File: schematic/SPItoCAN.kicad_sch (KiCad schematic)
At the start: 13 parts, among them J3 TB006-508-03BE, U17 MCP2515-I_SO, U2 ISO1050DUBR, Y1 CSTNE16M0V530000R0

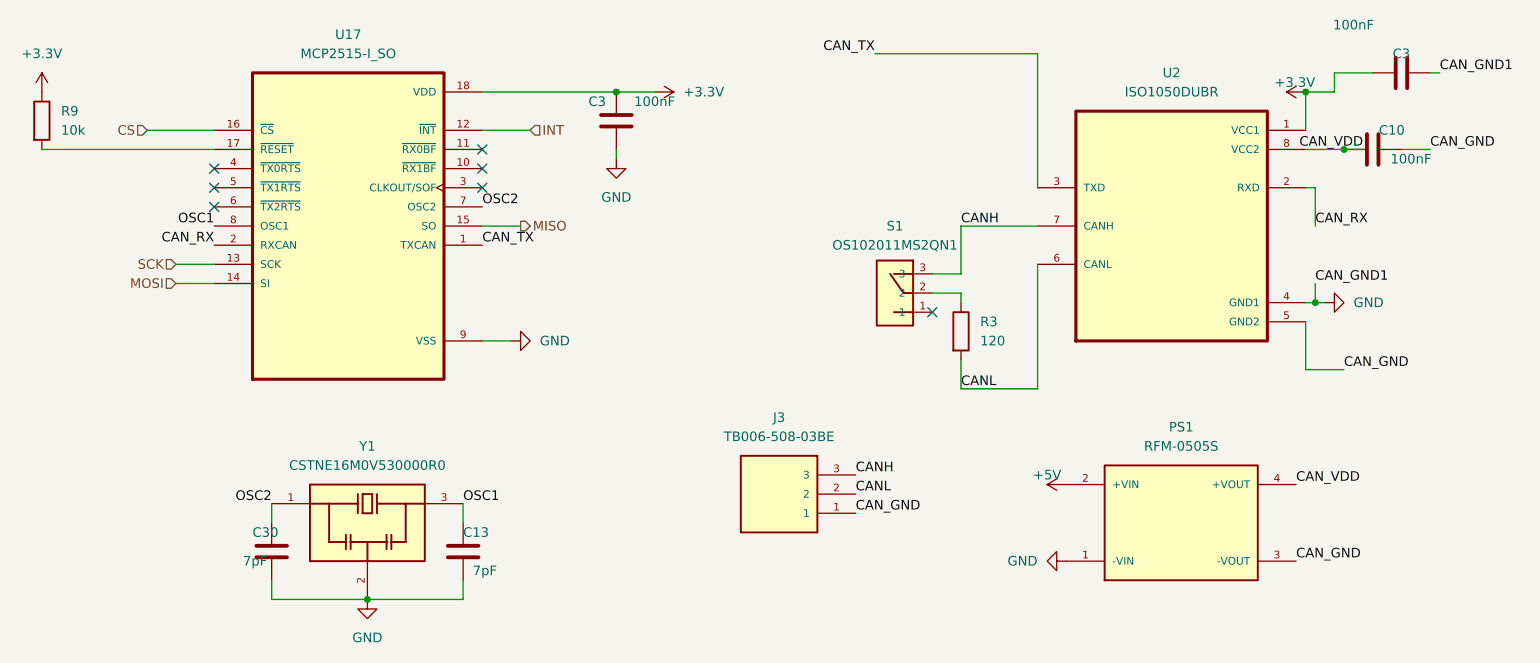
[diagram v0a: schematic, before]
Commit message: Changed to Kicad Version 8
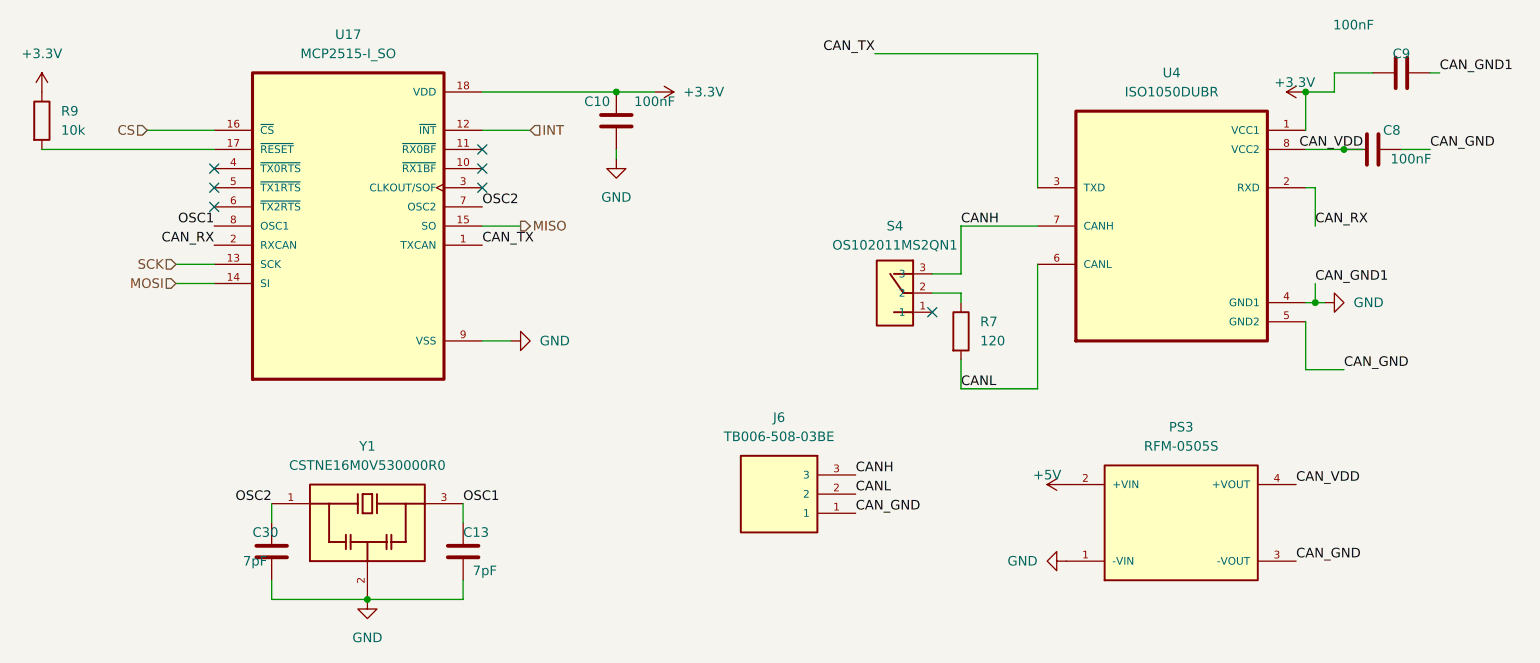
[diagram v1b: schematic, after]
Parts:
- renumbered C3 to C10, C10 to C8, C3 to C9, J3 to J6, PS1 to PS3, R3 to R7, S1 to S4, U2 to U4
